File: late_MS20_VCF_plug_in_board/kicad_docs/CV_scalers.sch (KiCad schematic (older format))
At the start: 11 parts, among them Q5 MMBT3906, Q6 MMBT3906, U3 TL072

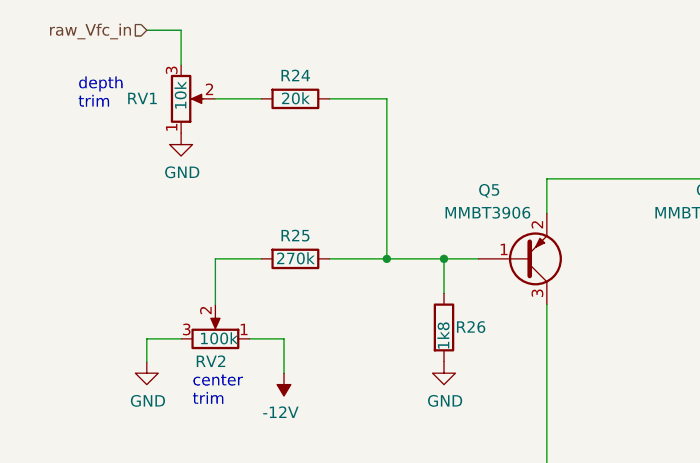
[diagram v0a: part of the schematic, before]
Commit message: change late MS20 CV scaling
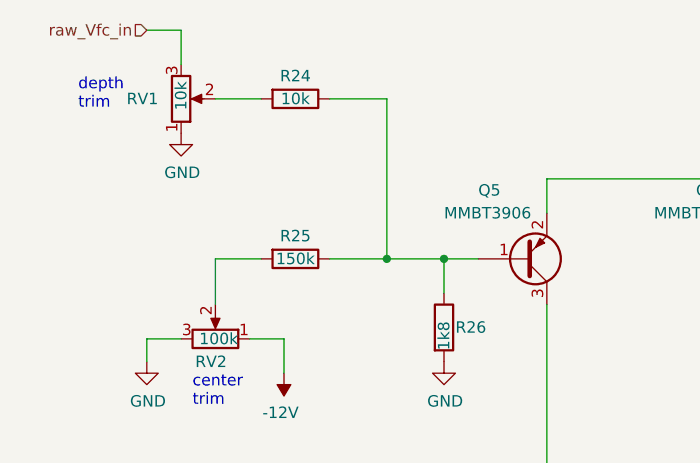
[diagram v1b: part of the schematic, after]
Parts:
- R24: value 20k -> 10k
- R25: value 270k -> 150k
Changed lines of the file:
@@
 AR Path="/5F326D3B/5F33DA85" Ref="R24"  Part="1"
 F 0 "R24" V 3950 2700 50  0000 C CNN
-F 1 "20k" V 4050 2700 50  0000 C CNN
+F 1 "10k" V 4050 2700 50  0000 C CNN
 F 2 "Resistor_SMD:R_0805_2012Metric_Pad1.15x1.40mm_HandSolder" V 3980 2700 50  0001 C CNN
 F 3 "~" H 4050 2700 50  0001 C CNN
@@
 AR Path="/5F326D3B/5F3E863C" Ref="R25"  Part="1"
 F 0 "R25" V 3950 3400 50  0000 C CNN
-F 1 "270k" V 4050 3400 50  0000 C CNN
+F 1 "150k" V 4050 3400 50  0000 C CNN
 F 2 "Resistor_SMD:R_0805_2012Metric_Pad1.15x1.40mm_HandSolder" V 3980 3400 50  0001 C CNN
 F 3 "~" H 4050 3400 50  0001 C CNN
